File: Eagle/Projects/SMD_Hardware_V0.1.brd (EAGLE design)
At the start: 63.2 x 50.8 mm, 35 parts, among them IC1 LM386M-1, Q1 12 MHz (ATS12A)

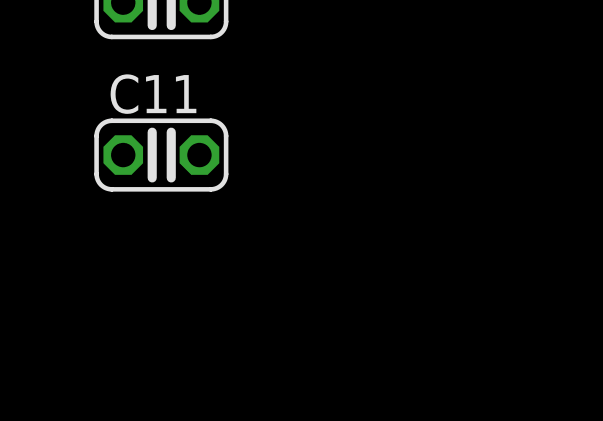
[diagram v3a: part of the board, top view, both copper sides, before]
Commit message: Updated the schematic a bit, lowered the ADC gain to not use digital gain.  Trying to improve the analog to take care of this
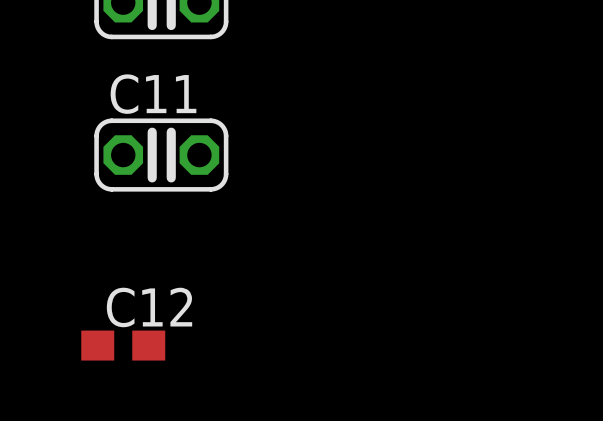
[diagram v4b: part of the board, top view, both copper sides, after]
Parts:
- added C12: 10uF, resistor:C0603
- C3: value (none) -> .05uF
- R8: value Rheostat -> 10k
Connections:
- net GND: now also C12.1, C12.2
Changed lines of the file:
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@@
 <element name="R6" library="resistor" package="R0603" value="10k" x="2.54" y="31.75"/>
 <element name="R7" library="resistor" package="R0603" value="10k" x="2.54" y="27.94"/>
-<element name="R8" library="resistor" package="R0603" value="Rheostat" x="2.54" y="24.13"/>
+<element name="R8" library="resistor" package="R0603" value="10k" x="2.54" y="24.13"/>
 <element name="R9" library="resistor" package="R0603" value="10k" x="2.54" y="20.32"/>
 <element name="R10" library="resistor" package="R0603" value="10k" x="2.54" y="13.97"/>
@@
 <attribute name="OC_NEWARK" value="25C3832" x="59.69" y="31.75" size="1.778" layer="27" display="off"/>
 </element>
-<element name="C3" library="resistor" package="C0603" value="" x="45.72" y="48.26" rot="R90"/>
+<element name="C3" library="resistor" package="C0603" value=".05uF" x="45.72" y="48.26" rot="R90"/>
 <element name="C5" library="resistor" package="140CLH-0810" value="220uF 25V" x="44.45" y="34.29" rot="R180"/>
 <element name="R12" library="resistor" package="R0603" value="10" x="31.75" y="49.53" rot="R180"/>
@@
 <element name="C10" library="resistor" package="C025-024X044" value="10pF" x="-10.16" y="-12.7"/>
 <element name="C11" library="resistor" package="C025-024X044" value="10pF" x="-10.16" y="-17.78"/>
+<element name="C12" library="resistor" package="C0603" value="10uF" x="-11.43" y="-24.13"/>
 </elements>
 <signals>
@@
 <contactref element="C11" pad="2"/>
 <contactref element="C10" pad="2"/>
+<contactref element="C12" pad="2"/>
+<contactref element="C12" pad="1"/>
 <wire x1="58.42" y1="31.75" x2="54.61" y2="43.18" width="0" layer="19" extent="1-1"/>
 <wire x1="32.6" y1="49.53" x2="54.61" y2="43.18" width="0" layer="19" extent="1-1"/>
@@
 <wire x1="-8.89" y1="-12.7" x2="2.12" y2="-2.54" width="0" layer="19" extent="1-1"/>
 <wire x1="-8.89" y1="-17.78" x2="-8.89" y2="-12.7" width="0" layer="19" extent="1-1"/>
+<wire x1="-10.58" y1="-24.13" x2="-8.89" y2="-17.78" width="0" layer="19" extent="1-1"/>
+<wire x1="-12.28" y1="-24.13" x2="-10.58" y2="-24.13" width="0" layer="19" extent="1-1"/>
 </signal>
 <signal name="N$1">

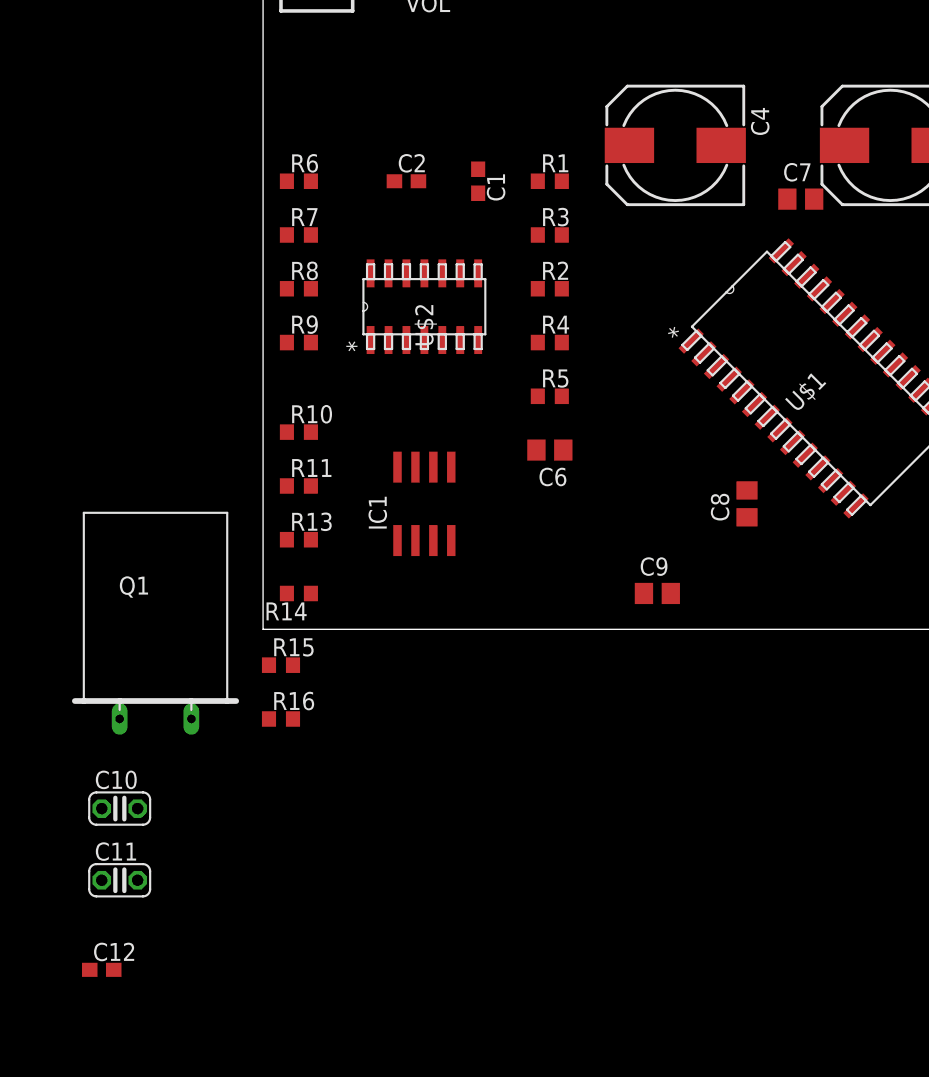
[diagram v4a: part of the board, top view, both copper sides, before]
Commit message: Cleaned up the schematic a bit and added an app note about anti-aliasing filters for ADC (which will need to be implemented)
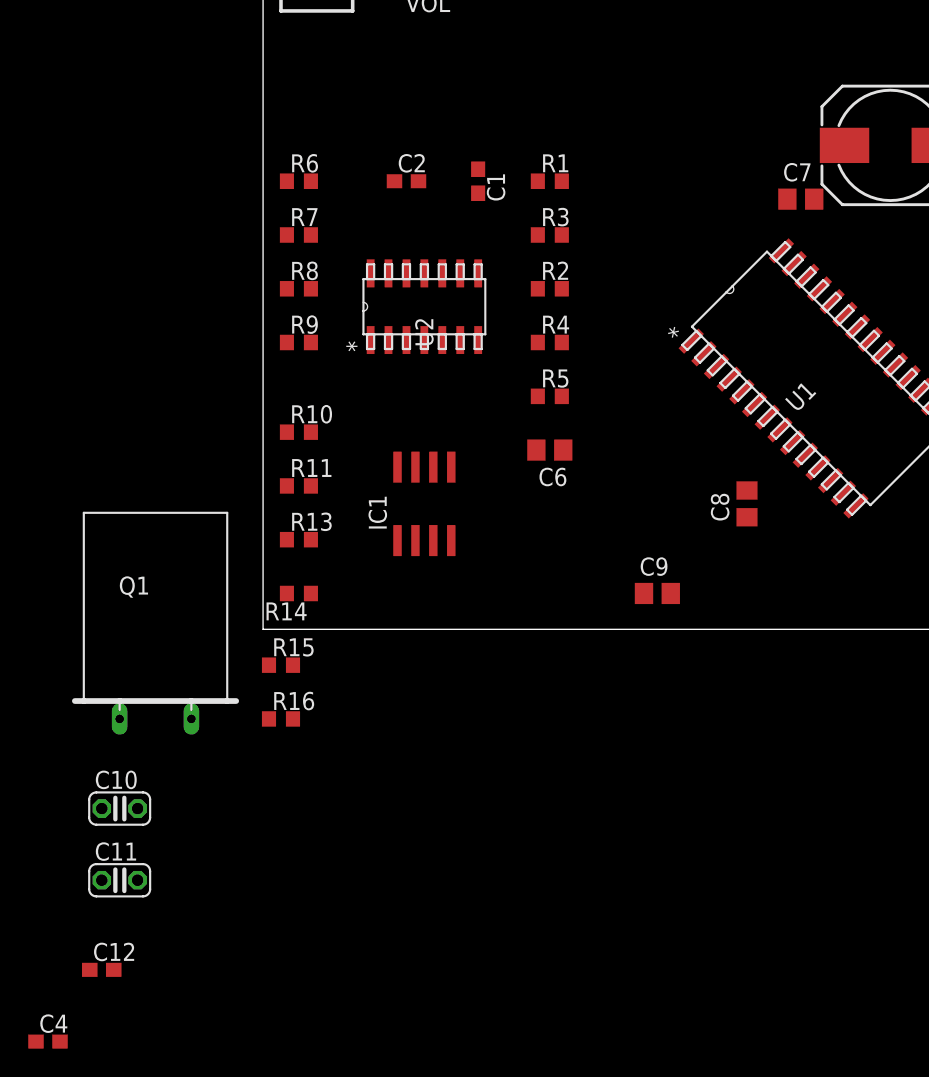
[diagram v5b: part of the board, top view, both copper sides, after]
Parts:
- C4: value .1uF 400V -> .1uF; device resistor:140CLH-0810 -> resistor:C0603
- R14: value 0 (short) -> 0
- moved C4 77.5 mm to (-15.2, -29.2), turned to 0 degrees
- renumbered U$1 to U1, U$2 to U2
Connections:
- removed net N$20: C8.2, U1.19, U1.8
- removed net N$26: C4.+, R15.1, R16.2, R3.2, U2.1
- removed net N$27: U1.4
- removed net N$6: U1.5
- new net N$30: C7.2, C8.2, U1.13, U1.28
- net GND: now also C7.1, C8.1, R16.1, U1.19, U1.27, U1.8; no longer R15.2
- net N$12: now also C4.1, R15.2, R16.2; no longer C4.-
- net N$19: now also U2.4; no longer C8.1, U1.13
- net N$21: now also R3.2, U2.1; no longer C7.1, U1.28
- net N$22: now also C4.2; no longer C7.2, U1.27
- net VDD: now also R15.1; no longer R16.1, U2.4
